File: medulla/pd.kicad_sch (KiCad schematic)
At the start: 19 parts, among them U1 LM2678S-12, U2 LM2678S-5.0

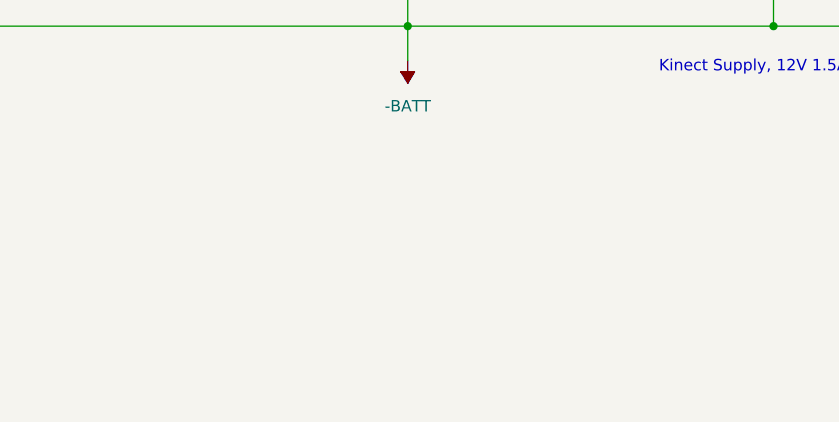
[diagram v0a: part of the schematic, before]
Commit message: alpha 0.2.0: Added RP2040, LM2936-3.3V Regulator, removed ADS1115, PCA9685
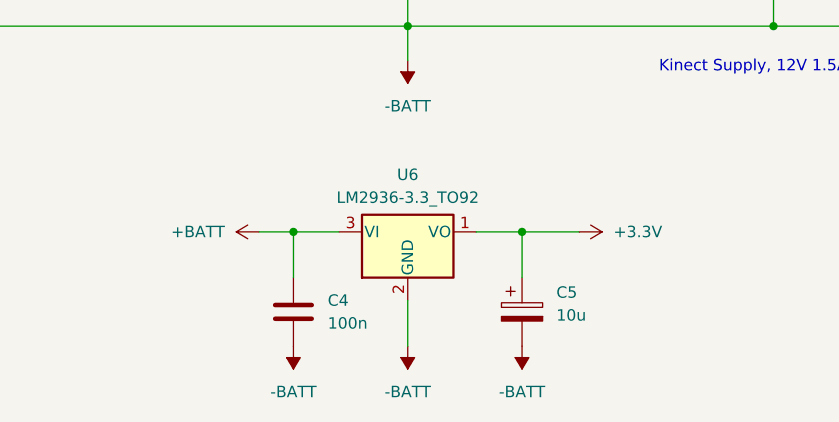
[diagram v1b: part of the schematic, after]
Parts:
- added C4: 100n, symbol Device:C
- added C5: 10u, symbol Device:C_Polarized
- added U6: LM2936-3.3_TO92, Package_TO_SOT_THT:TO-92_Inline, symbol Regulator_Linear:LM2936-3.3_TO92
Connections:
- net +BATT: now also C4.1, U6.3 (VI)
- net -BATT: now also C4.2, C5.2, U6.2 (GND)
- new net +3.3V: C5.1, U6.1 (VO)
